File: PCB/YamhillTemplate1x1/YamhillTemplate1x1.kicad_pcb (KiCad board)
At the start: 2 copper layers, 6 parts

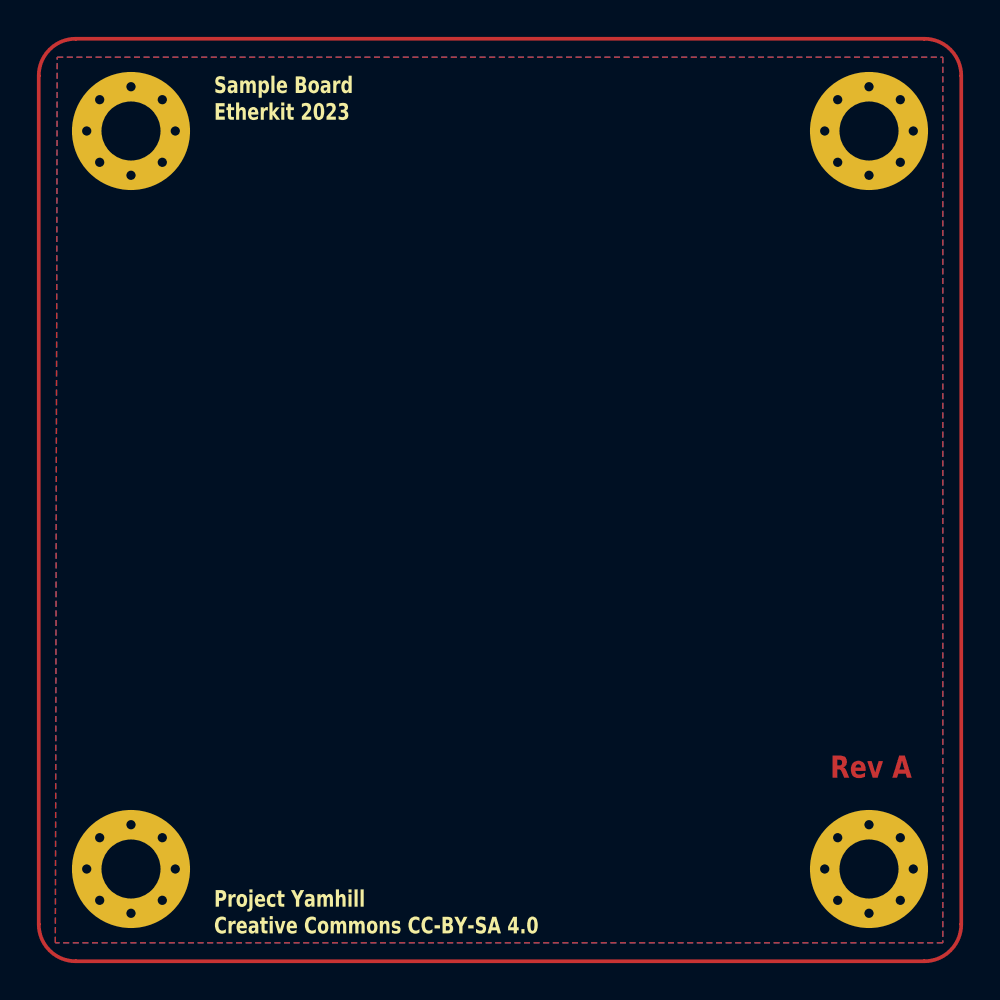
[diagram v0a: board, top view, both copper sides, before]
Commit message: Fix PCB template problems
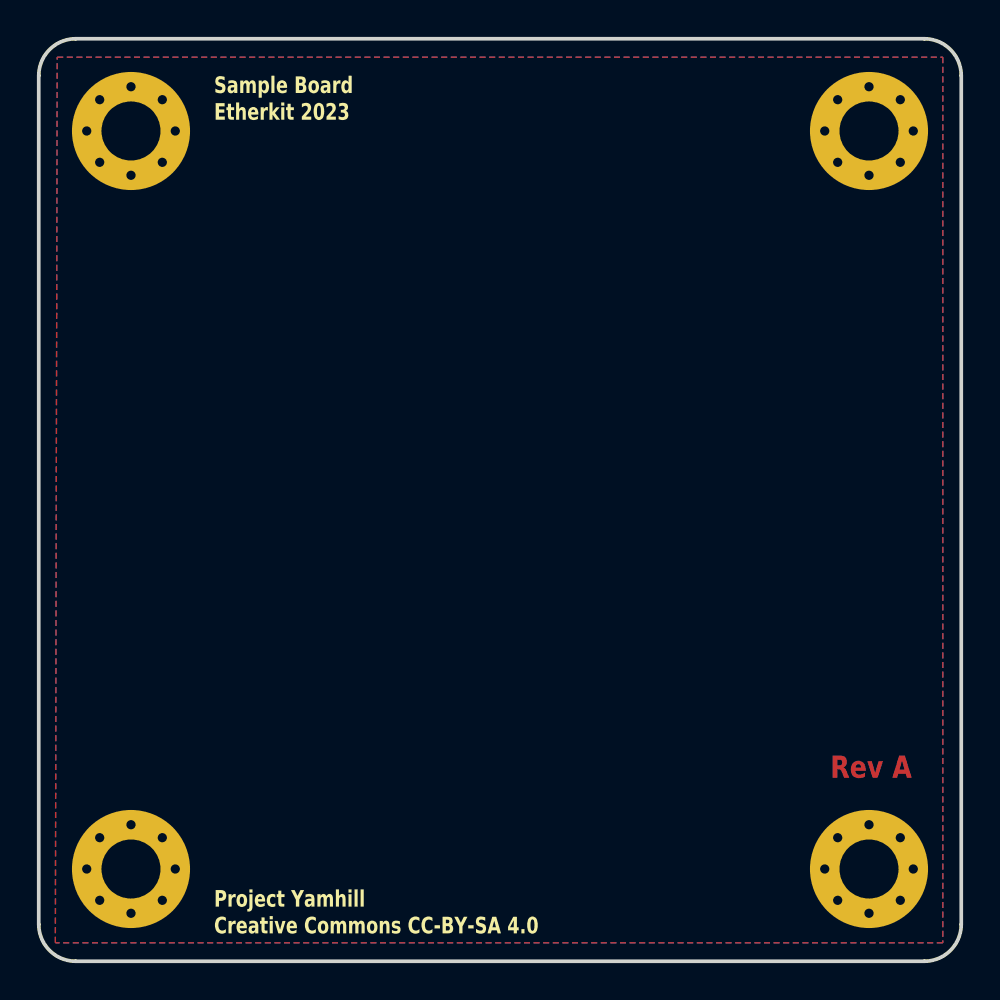
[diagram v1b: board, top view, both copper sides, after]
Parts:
- removed REF** (x4): MountingHole_3.2mm_M3_Pad_Via, MountingHole:MountingHole_3.2mm_M3_Pad_Via
- added H1: MountingHole_Pad, MountingHole:MountingHole_3.2mm_M3_Pad_Via, F.Cu at (105.0, 55.0)
- added H2: MountingHole_Pad, MountingHole:MountingHole_3.2mm_M3_Pad_Via, F.Cu at (145.0, 55.0)
- added H3: MountingHole_Pad, MountingHole:MountingHole_3.2mm_M3_Pad_Via, F.Cu at (105.0, 95.0)
- added H4: MountingHole_Pad, MountingHole:MountingHole_3.2mm_M3_Pad_Via, F.Cu at (145.0, 95.0)
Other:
- board outline added: 50 x 50 mm

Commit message: Update 1x1 template
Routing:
- net (no net): vias 0 -> 40
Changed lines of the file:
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@@
     (effects (font (size 1.2 1) (thickness 0.25) bold) (justify left bottom))
   )
-  (gr_text "Project Yamhill\nCreative Commons CC-BY-SA 4.0" (at 109.5 98.6) (layer "F.SilkS")
+  (gr_text "Project Yamhill\nCreative Commons CC-BY-SA 4.0" (at 109 97.7) (layer "F.SilkS")
     (effects (font (size 0.9 0.7) (thickness 0.175) bold) (justify left bottom))
   )
-  (gr_text "Sample Board\nEtherkit 2023" (at 109.5 54.5) (layer "F.SilkS")
+  (gr_text "Sample Board\nEtherkit 2023" (at 109.3 54.9) (layer "F.SilkS")
     (effects (font (size 0.9 0.7) (thickness 0.175) bold) (justify left bottom))
   )
-  (zone (net 0) (net_name "") (layers "F&B.Cu") (name "Ground Plane") (hatch edge 0.5)
-    (connect_pads (clearance 0.5))
-    (min_thickness 0.25) (filled_areas_thickness no)
+  (via (at 122 51) (size 0.4) (drill 0.2) (layers "F.Cu" "B.Cu") (net 0))
+  (via (at 101 82) (size 0.4) (drill 0.2) (layers "F.Cu" "B.Cu") (net 0))
+  (via (at 149 82) (size 0.4) (drill 0.2) (layers "F.Cu" "B.Cu") (net 0))
+  (via (at 149 97) (size 0.4) (drill 0.2) (layers "F.Cu" "B.Cu") (net 0))
+  (via (at 147 51) (size 0.4) (drill 0.2) (layers "F.Cu" "B.Cu") (net 0))
+  (via (at 149 72) (size 0.4) (drill 0.2) (layers "F.Cu" "B.Cu") (net 0))
+  (via (at 149 62) (size 0.4) (drill 0.2) (layers "F.Cu" "B.Cu") (net 0))
+  (via (at 117 99) (size 0.4) (drill 0.2) (layers "F.Cu" "B.Cu") (net 0))
+  (via (at 142 51) (size 0.4) (drill 0.2) (layers "F.Cu" "B.Cu") (net 0))
+  (via (at 149 77) (size 0.4) (drill 0.2) (layers "F.Cu" "B.Cu") (net 0))
+  (via (at 149 57) (size 0.4) (drill 0.2) (layers "F.Cu" "B.Cu") (net 0))
+  (via (at 101 87) (size 0.4) (drill 0.2) (layers "F.Cu" "B.Cu") (net 0))
+  (via (at 149 52) (size 0.4) (drill 0.2) (layers "F.Cu" "B.Cu") (net 0))
+  (via (at 132 51) (size 0.4) (drill 0.2) (layers "F.Cu" "B.Cu") (net 0))
+  (via (at 101 52) (size 0.4) (drill 0.2) (layers "F.Cu" "B.Cu") (net 0))
+  (via (at 107 51) (size 0.4) (drill 0.2) (layers "F.Cu" "B.Cu") (net 0))
+  (via (at 101 97) (size 0.4) (drill 0.2) (layers "F.Cu" "B.Cu") (net 0))
+  (via (at 149 67) (size 0.4) (drill 0.2) (layers "F.Cu" "B.Cu") (net 0))
+  (via (at 107 99) (size 0.4) (drill 0.2) (layers "F.Cu" "B.Cu") (net 0))
+  (via (at 101 67) (size 0.4) (drill 0.2) (layers "F.Cu" "B.Cu") (net 0))
+  (via (at 149 87) (size 0.4) (drill 0.2) (layers "F.Cu" "B.Cu") (net 0))
+  (via (at 102 51) (size 0.4) (drill 0.2) (layers "F.Cu" "B.Cu") (net 0))
+  (via (at 122 99) (size 0.4) (drill 0.2) (layers "F.Cu" "B.Cu") (net 0))
+  (via (at 101 77) (size 0.4) (drill 0.2) (layers "F.Cu" "B.Cu") (net 0))
+  (via (at 112 51) (size 0.4) (drill 0.2) (layers "F.Cu" "B.Cu") (net 0))
+  (via (at 142 99) (size 0.4) (drill 0.2) (layers "F.Cu" "B.Cu") (net 0))
+  (via (at 127 99) (size 0.4) (drill 0.2) (layers "F.Cu" "B.Cu") (net 0))
+  (via (at 127 51) (size 0.4) (drill 0.2) (layers "F.Cu" "B.Cu") (net 0))
+  (via (at 137 99) (size 0.4) (drill 0.2) (layers "F.Cu" "B.Cu") (net 0))
+  (via (at 101 62) (size 0.4) (drill 0.2) (layers "F.Cu" "B.Cu") (net 0))
+  (via (at 137 51) (size 0.4) (drill 0.2) (layers "F.Cu" "B.Cu") (net 0))
+  (via (at 101 57) (size 0.4) (drill 0.2) (layers "F.Cu" "B.Cu") (net 0))
+  (via (at 112 99) (size 0.4) (drill 0.2) (layers "F.Cu" "B.Cu") (net 0))
+  (via (at 147 99) (size 0.4) (drill 0.2) (layers "F.Cu" "B.Cu") (net 0))
+  (via (at 102 99) (size 0.4) (drill 0.2) (layers "F.Cu" "B.Cu") (net 0))
+  (via (at 101 72) (size 0.4) (drill 0.2) (layers "F.Cu" "B.Cu") (net 0))
+  (via (at 117 51) (size 0.4) (drill 0.2) (layers "F.Cu" "B.Cu") (net 0))
+  (via (at 101 92) (size 0.4) (drill 0.2) (layers "F.Cu" "B.Cu") (net 0))
+  (via (at 132 99) (size 0.4) (drill 0.2) (layers "F.Cu" "B.Cu") (net 0))
+  (via (at 149 92) (size 0.4) (drill 0.2) (layers "F.Cu" "B.Cu") (net 0))
+  (zone locked (net 0) (net_name "") (layers "F&B.Cu") (name "Ground Plane") (hatch edge 0.5)
+    (connect_pads (clearance 0.15))
+    (min_thickness 0.15) (filled_areas_thickness no)
     (fill (thermal_gap 0.5) (thermal_bridge_width 0.5) (smoothing chamfer) (radius 1) (island_removal_mode 1) (island_area_min 10))
     (polygon
       (pts
-        (xy 101 51)
-        (xy 149 51)
-        (xy 149 99)
-        (xy 100.9 99)
+        (xy 99.974457 49.974457)
+        (xy 149.972139 50.027861)
+        (xy 149.966772 99.966772)
+        (xy 100 100)
       )
     )
+  )
+  (zone (net 0) (net_name "") (layers "*.Mask") (hatch full 0.5)
+    (connect_pads (clearance 0.5))
+    (min_thickness 0.25) (filled_areas_thickness no)
+    (fill (thermal_gap 0.5) (thermal_bridge_width 0.5))
+    (polygon
+      (pts
+        (xy 100 98)
+        (xy 102 98)
+        (xy 102 52)
+        (xy 100 52)
+      )
+    )
+  )
+  (zone (net 0) (net_name "") (layers "*.Mask") (hatch full 0.5)
+    (connect_pads (clearance 0.5))
+    (min_thickness 0.25) (filled_areas_thickness no)
+    (fill (thermal_gap 0.5) (thermal_bridge_width 0.5))
+    (polygon
+      (pts
+        (xy 100 100)
+        (xy 100 98)
+        (xy 150 98)
+        (xy 150 100)
+      )
+    )
+  )
+  (zone (net 0) (net_name "") (layers "*.Mask") (hatch full 0.5)
+    (connect_pads (clearance 0.5))
+    (min_thickness 0.25) (filled_areas_thickness no)
+    (fill (thermal_gap 0.5) (thermal_bridge_width 0.5))
+    (polygon
+      (pts
+        (xy 150 98)
+        (xy 148 98)
+        (xy 148 52)
+        (xy 150 52)
+      )
+    )
+  )
+  (zone (net 0) (net_name "") (layers "*.Mask") (hatch full 0.5)
+    (connect_pads (clearance 0.5))
+    (min_thickness 0.25) (filled_areas_thickness no)
+    (fill (thermal_gap 0.5) (thermal_bridge_width 0.5))
+    (polygon
+      (pts
+        (xy 100 50)
+        (xy 150 50)
+        (xy 150 52)
+        (xy 100 52)
+      )
+    )

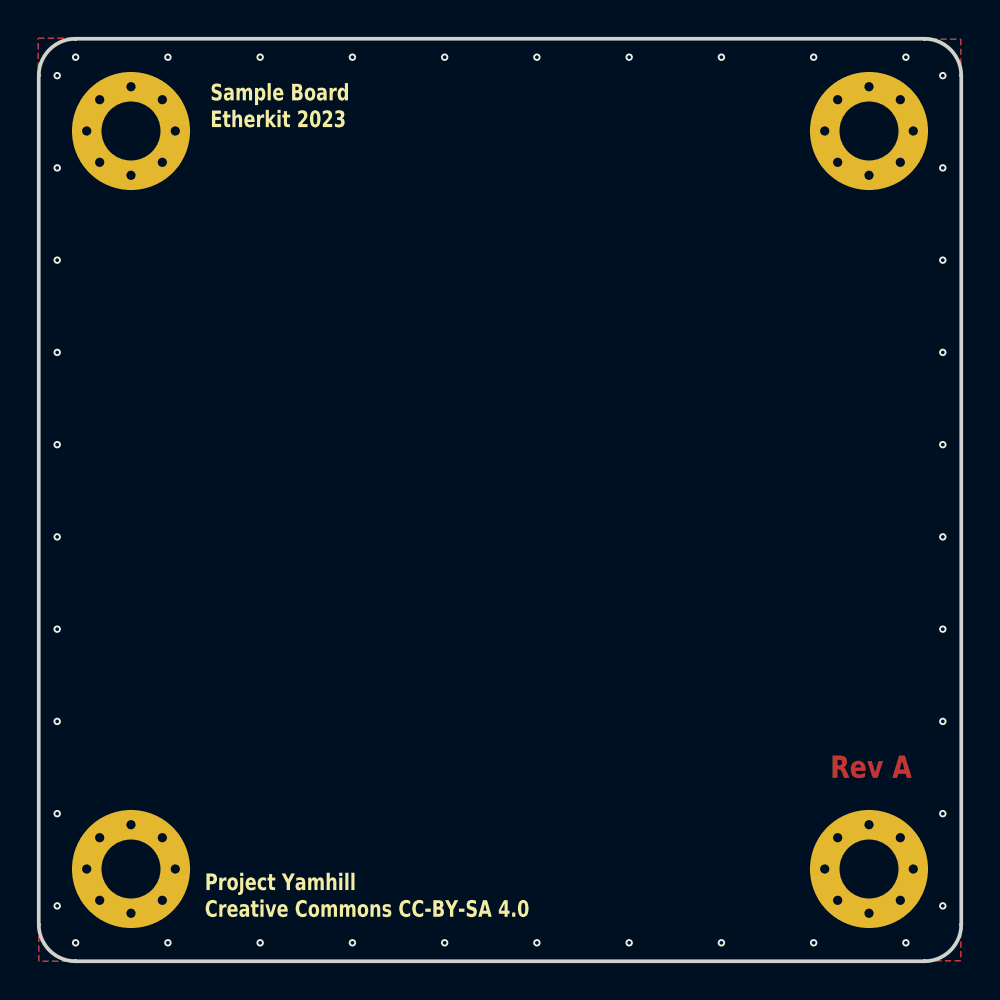
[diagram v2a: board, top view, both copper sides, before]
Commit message: Add Diode Ring Mixer Board
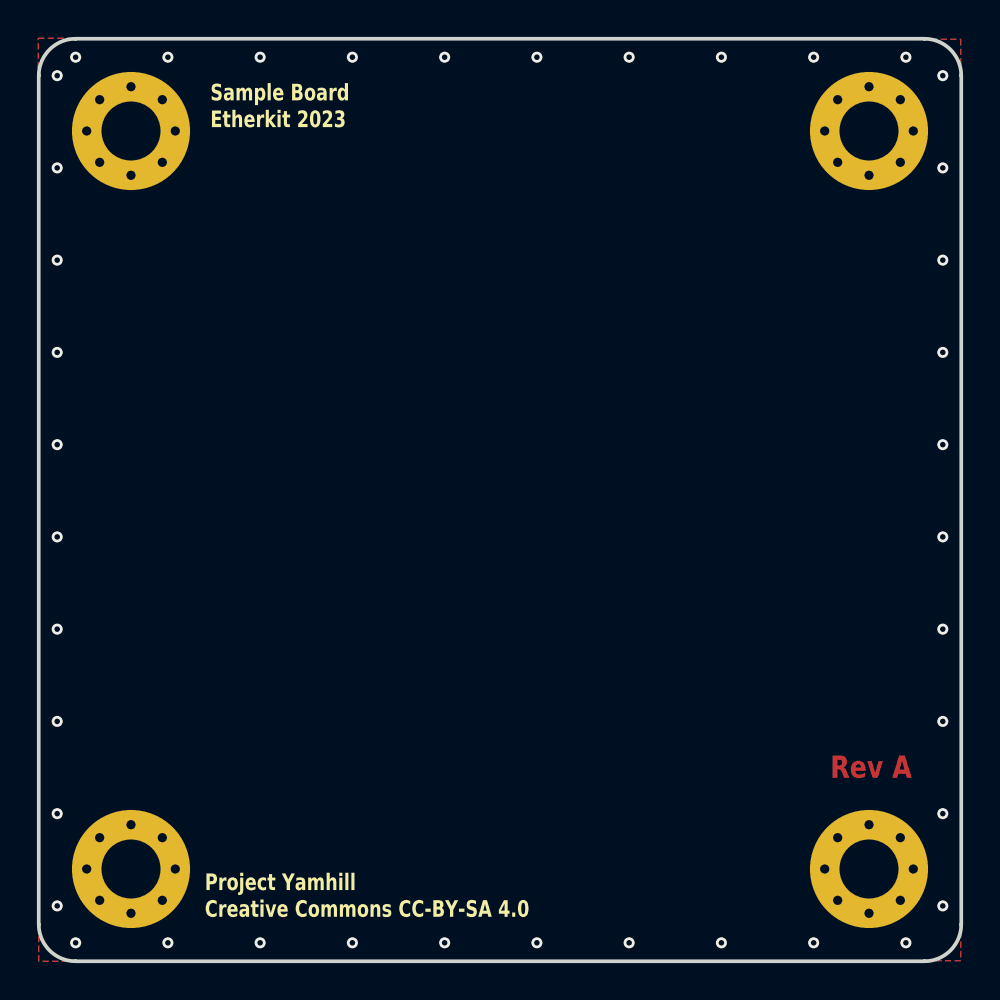
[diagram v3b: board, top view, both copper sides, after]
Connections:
- H1 pad 1: unconnected-(H1-Pad1) -> GND
- H2 pad 1: unconnected-(H2-Pad1) -> GND
- H3 pad 1: unconnected-(H3-Pad1) -> GND
- H4 pad 1: unconnected-(H4-Pad1) -> GND
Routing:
- net GND: vias 0 -> 40
- net (no net): vias 40 -> 0
